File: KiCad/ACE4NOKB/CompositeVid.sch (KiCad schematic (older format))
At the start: 36 parts, among them Q1 2N3904, Q100 2N3904, X1 CRYSTALHC49U-V 6.556MHz

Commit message: Double check transistors
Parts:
- Q1: footprint Package_TO_SOT_THT:TO-92_Inline -> Package_TO_SOT_THT:TO-92L_Inline
- Q100: footprint Package_TO_SOT_THT:TO-92L_HandSolder -> Package_TO_SOT_THT:TO-92L_Inline
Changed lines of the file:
@@
 F 0 "Q100" H 14250 3325 50  0000 L BNN
 F 1 "2N3904" H 14050 3225 50  0000 L BNN
-F 2 "Package_TO_SOT_THT:TO-92L_HandSolder" H 14450 3325 50  0001 C CNN
-F 3 "" H 14450 3325 50  0001 C CNN
+F 2 "Package_TO_SOT_THT:TO-92L_Inline" H 14450 3325 50  0001 C CNN
+F 3 "https://www.onsemi.com/pub/Collateral/PZT3904-D.pdf" H 14450 3325 50  0001 C CNN
 	1    14450 3325
 	1    0    0    -1
@@
 F 0 "Q1" H 5205 8585 50  0000 L CNN
 F 1 "2N3904" H 5190 8820 50  0000 L CNN
-F 2 "Package_TO_SOT_THT:TO-92_Inline" H 5600 8600 50  0001 L CIN
-F 3 "https:~/www.fairchildsemi.com/datasheets/2N/2N3904.pdf" H 5400 8675 50  0001 L CNN
+F 2 "Package_TO_SOT_THT:TO-92L_Inline" H 5600 8600 50  0001 L CIN
+F 3 "https://www.onsemi.com/pub/Collateral/PZT3904-D.pdf" H 5400 8675 50  0001 L CNN
 	1    5400 8675
 	1    0    0    -1

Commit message: Update IO port decoding.
Signed-off-by: John Bradley <flypie@rocketmail.com>
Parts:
- X1: value CRYSTALHC49U-V 6.556MHz -> CRYSTALHC49U-V 6.5MHz
- Z102: value 74AHCT04 -> SN74AHCT04N
- Z27: value 74AHCT74 -> SN74AHCT74N
- renumbered R102 to R108
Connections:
- wire segments 275 -> 274

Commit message: re order pcbs and some logic. Move transistor
Signed-off-by: John Bradley <flypie@rocketmail.com>
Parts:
- Z5-6, Z7-8: symbol 7132la100pdg:IDT71321 -> ACE4NOKB-rescue:IDT71321-7132la100pdg
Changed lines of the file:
@@
 EESchema Schematic File Version 4
 LIBS:ACE4NOKB-cache
-LIBS:ear-cache
 EELAYER 30 0
 EELAYER END
 $Descr A3 16535 11693
 encoding utf-8
-Sheet 3 4
+Sheet 2 4
 Title "JupiterAceZ180"
 Date "2019-08-26"
@@
 $EndComp
 $Comp
-L 7132la100pdg:IDT71321 Z7-8
+L ACE4NOKB-rescue:IDT71321-7132la100pdg Z7-8
 U 1 1 5F80C938
 P 11775 4625
@@
 $EndComp
 $Comp
-L 7132la100pdg:IDT71321 Z5-6
+L ACE4NOKB-rescue:IDT71321-7132la100pdg Z5-6
 U 1 1 5F80C942
 P 9175 5225

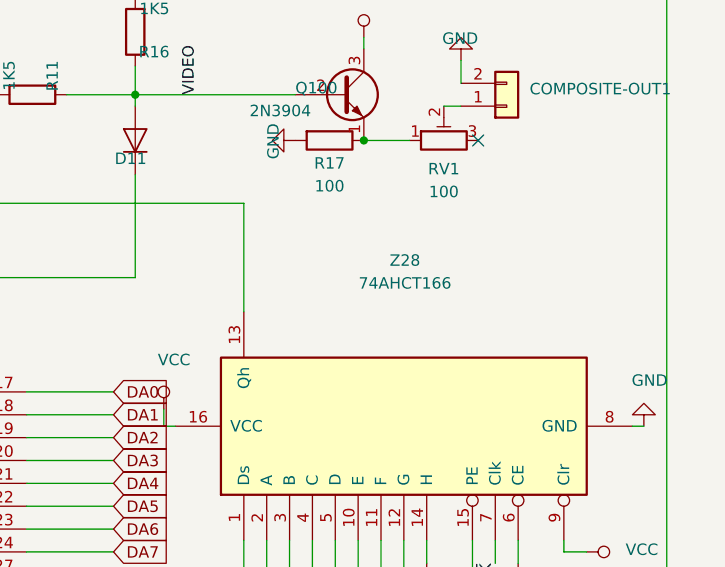
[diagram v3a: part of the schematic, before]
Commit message: Candidate MMU Schematic. ACE4NOKB.
Signed-off-by: John Bradley <flypie@rocketmail.com>
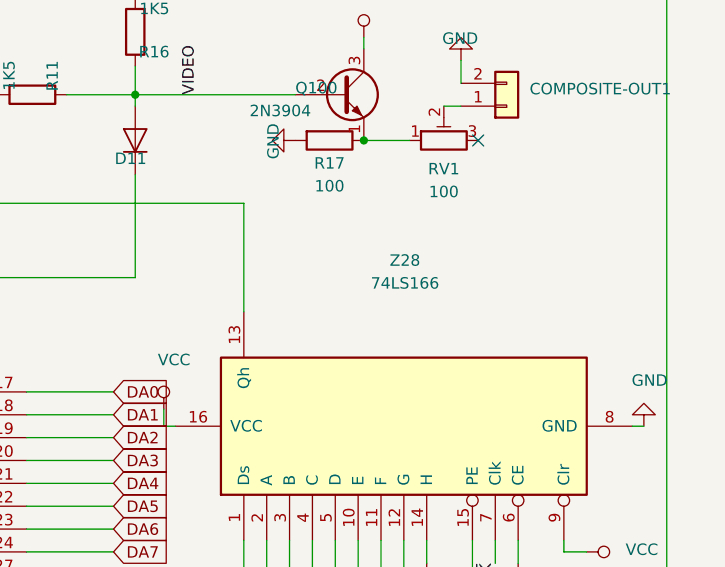
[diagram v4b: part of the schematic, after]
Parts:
- Z28: value 74AHCT166 -> 74LS166
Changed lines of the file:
@@
-$EndComp
-$Comp
-L 74xx:74LS166 Z28
-U 1 1 5F80C89E
-P 14725 4775
-F 0 "Z28" V 15450 4770 50  0000 C CNN
-F 1 "74AHCT166" V 15350 4770 50  0000 C CNN
-F 2 "Package_DIP:DIP-16_W7.62mm" H 14725 4775 50  0001 C CNN
-F 3 "http:/www.ti.com/lit/gpn/sn74AHCT166" H 14725 4775 50  0001 C CNN
-	1    14725 4775
-	0    -1   -1   0
 $EndComp
 $Comp
@@
 	1    0    0    -1
 $EndComp
+$Comp
+L 74xx:74LS166 Z28
+U 1 1 5F80C89E
+P 14725 4775
+F 0 "Z28" V 15450 4770 50  0000 C CNN
+F 1 "74LS166" V 15350 4770 50  0000 C CNN
+F 2 "Package_DIP:DIP-16_W7.62mm" H 14725 4775 50  0001 C CNN
+F 3 "http:/www.ti.com/lit/gpn/sn74ALS166" H 14725 4775 50  0001 C CNN
+	1    14725 4775
+	0    -1   -1   0
+$EndComp
 $EndSCHEMATC

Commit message: Latest changes fix Diode misake in 2NOKB.
Signed-off-by: John Bradley <flypie@rocketmail.com>
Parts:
- removed unit 3 of Z23
- added unit 6 of Z102
- Z5-6, Z7-8: symbol ACE4NOKB-rescue:IDT71321-7132la100pdg -> 7132la100pdg:IDT71321-421-52PIN-PLCC
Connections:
- net ~VIDEOCLK: now also Z102.12
- net at R100.2: no longer Z5-6.4 (~INTL)
- net at R101.2: no longer Z5-6.48 (~INTR)
- net at R104.2: no longer Z7-8.4 (~INTL)
- net at R105.2: no longer Z7-8.48 (~INTR)
- net at C1.1, Q1.3 (C), R1.2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: now also Z102.13
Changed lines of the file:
@@
 EESchema Schematic File Version 4
-LIBS:ACE4NOKB-cache
 EELAYER 30 0
 EELAYER END
@@
 $EndComp
 $Comp
-L ACE4NOKB-rescue:IDT71321-7132la100pdg Z7-8
+L 7132la100pdg:IDT71321-421-52PIN-PLCC Z7-8
 U 1 1 5F80C938
 P 11775 4625
@@
 $EndComp
 $Comp
-L ACE4NOKB-rescue:IDT71321-7132la100pdg Z5-6
+L 7132la100pdg:IDT71321-421-52PIN-PLCC Z5-6
 U 1 1 5F80C942
 P 9175 5225
@@
 $EndComp
 Wire Wire Line
-	6400 8575 6475 8575
+	6400 8475 6475 8475
 Wire Wire Line
 	5100 8475 5500 8475
@@
 	0    1    1    0
 $EndComp
-$Comp
-L power:GND #0125
-U 1 1 5F80CE33
-P 5700 8675
-F 0 "#0125" H 5700 8425 50  0001 C CNN
-F 1 "GND" H 5710 8495 50  0000 C CNN
-F 2 "" H 5700 8675 50  0001 C CNN
-F 3 "" H 5700 8675 50  0001 C CNN
-	1    5700 8675
-	1    0    0    -1
-$EndComp
-$Comp
-L 74xx:74LS86 Z23
-U 3 1 5F80CE2D
-P 6100 8575
-F 0 "Z23" H 6100 8925 50  0000 C CNN
-F 1 "74AHCT86" H 6100 8825 50  0000 C CNN
-F 2 "Package_DIP:DIP-14_W7.62mm" H 6100 8575 50  0001 C CNN
-F 3 "74xx~74AHCT86.pdf" H 6100 8575 50  0001 C CNN
-	3    6100 8575
-	1    0    0    -1
-$EndComp
 Wire Wire Line
 	4700 8675 5200 8675
@@
 	4700 8475 4800 8475
 Wire Wire Line
-	5700 8675 5800 8675
-Wire Wire Line
 	5500 8875 5500 8975
 Wire Wire Line
@@
 Wire Wire Line
 	15875 5475 15875 2225
-Text Label 6475 8575 0    50   ~ 0
+Text Label 6475 8475 0    50   ~ 0
 ~VIDEOCLK
 Text Label 9950 3025 2    50   ~ 0
@@
 	0    -1   -1   0
 $EndComp
+$Comp
+L 74xx:74LS04 Z?
+U 6 1 5E5B189A
+P 6100 8475
+AR Path="/5E5B189A" Ref="Z?"  Part="6"
+AR Path="/5E2F9A69/5E5B189A" Ref="Z102"  Part="6"
+F 0 "Z102" H 6100 8825 50  0000 C CNN
+F 1 "SN74AHCT04N" H 6100 8725 50  0000 C CNN
+F 2 "Package_DIP:DIP-14_W7.62mm" H 6100 8475 50  0001 C CNN
+F 3 "http://www.ti.com/lit/gpn/sn74LS04" H 6100 8475 50  0001 C CNN
+	6    6100 8475
+	1    0    0    -1
+$EndComp
 $EndSCHEMATC

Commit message: Reorder chematics.
Signed-off-by: John Bradley <flypie@rocketmail.com>
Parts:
- removed Z10, Z11, Z9: 74AHCT393, Package_DIP:DIP-14_W7.62mm, symbol 74xx:74LS393
- removed unit 1 of Z20
- removed Z21: 74AHCT11, Package_DIP:DIP-14_W7.62mm, symbol 74xx:74LS11
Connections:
- net 50Hz: now reaches Z102.9, Z25.6
- no-connect marks 8 -> 2
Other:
- moved on the sheet: C1, C2, Q1, R1, R2, X1, Z102F
